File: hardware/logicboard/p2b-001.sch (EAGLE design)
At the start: 61 parts, among them IC1 74LS06N, IC2 4066N, J1 MKR, J2 GPIO, J3 Vcc, J4 RLY, J5 SPI, J6 LED, J7 DIN5, J8 DIN5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

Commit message: Signal name.
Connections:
- net N$4 renamed CAP1N
- net N$5 renamed CAP1P
- net N$7 renamed LCDVOUT
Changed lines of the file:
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@@
 </segment>
 </net>
-<net name="N$4" class="0">
+<net name="CAP1N" class="0">
 <segment>
 <pinref part="LCD1" gate="G$1" pin="3"/>
 <wire x1="332.74" y1="88.9" x2="358.14" y2="88.9" width="0.1524" layer="91"/>
 <pinref part="C12" gate="G$1" pin="2"/>
+<label x="345.44" y="88.9" size="1.778" layer="95"/>
 </segment>
 </net>
-<net name="N$5" class="0">
+<net name="CAP1P" class="0">
 <segment>
 <pinref part="LCD1" gate="G$1" pin="4"/>
@@
 <wire x1="322.58" y1="88.9" x2="325.12" y2="88.9" width="0.1524" layer="91"/>
 <pinref part="C12" gate="G$1" pin="1"/>
+<label x="345.44" y="86.36" size="1.778" layer="95"/>
 </segment>
 </net>
-<net name="N$7" class="0">
+<net name="LCDVOUT" class="0">
 <segment>
 <wire x1="332.74" y1="93.98" x2="335.28" y2="93.98" width="0.1524" layer="91"/>
@@
 <wire x1="335.28" y1="91.44" x2="358.14" y2="91.44" width="0.1524" layer="91"/>
 <pinref part="C13" gate="G$1" pin="2"/>
+<label x="345.44" y="91.44" size="1.778" layer="95"/>
 </segment>
 </net>

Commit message: Silk.
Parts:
- R101, R102: value (none) -> 10k
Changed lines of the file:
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@@
 <part name="JP7" library="pinhead" library_urn="urn:adsk.eagle:library:325" deviceset="PINHD-1X4" device="" package3d_urn="urn:adsk.eagle:package:22407/2" value="MNTR"/>
 <part name="LCD1" library="AQM0802A-RN-GBW" deviceset="AQM0802A-RN-GBW" device=""/>
-<part name="R101" library="rcl" library_urn="urn:adsk.eagle:library:334" deviceset="R-EU_" device="M2012" package3d_urn="urn:adsk.eagle:package:23561/2"/>
-<part name="R102" library="rcl" library_urn="urn:adsk.eagle:library:334" deviceset="R-EU_" device="M2012" package3d_urn="urn:adsk.eagle:package:23561/2"/>
+<part name="R101" library="rcl" library_urn="urn:adsk.eagle:library:334" deviceset="R-EU_" device="M2012" package3d_urn="urn:adsk.eagle:package:23561/2" value="10k"/>
+<part name="R102" library="rcl" library_urn="urn:adsk.eagle:library:334" deviceset="R-EU_" device="M2012" package3d_urn="urn:adsk.eagle:package:23561/2" value="10k"/>
 <part name="SUPPLY20" library="supply2" deviceset="GND" device=""/>
 <part name="C11" library="rcl" library_urn="urn:adsk.eagle:library:334" deviceset="C-EU" device="025-024X044" package3d_urn="urn:adsk.eagle:package:23630/1" value="100n"/>

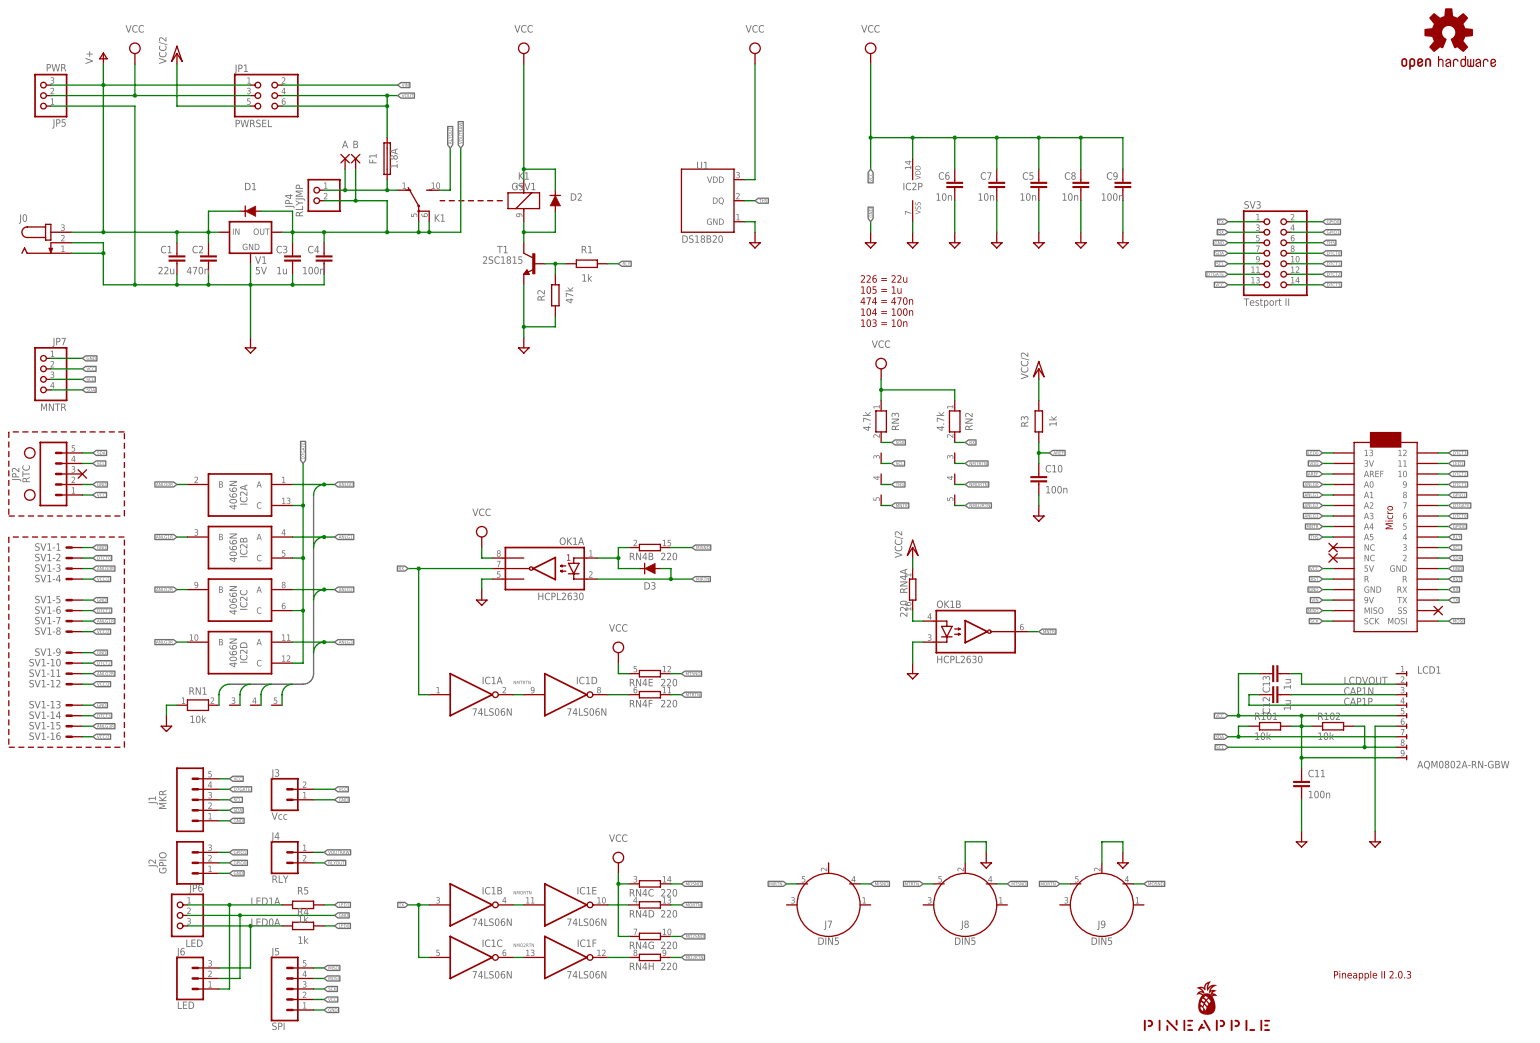
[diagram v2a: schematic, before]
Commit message: Now LCD runs on 5V or 3.3V.
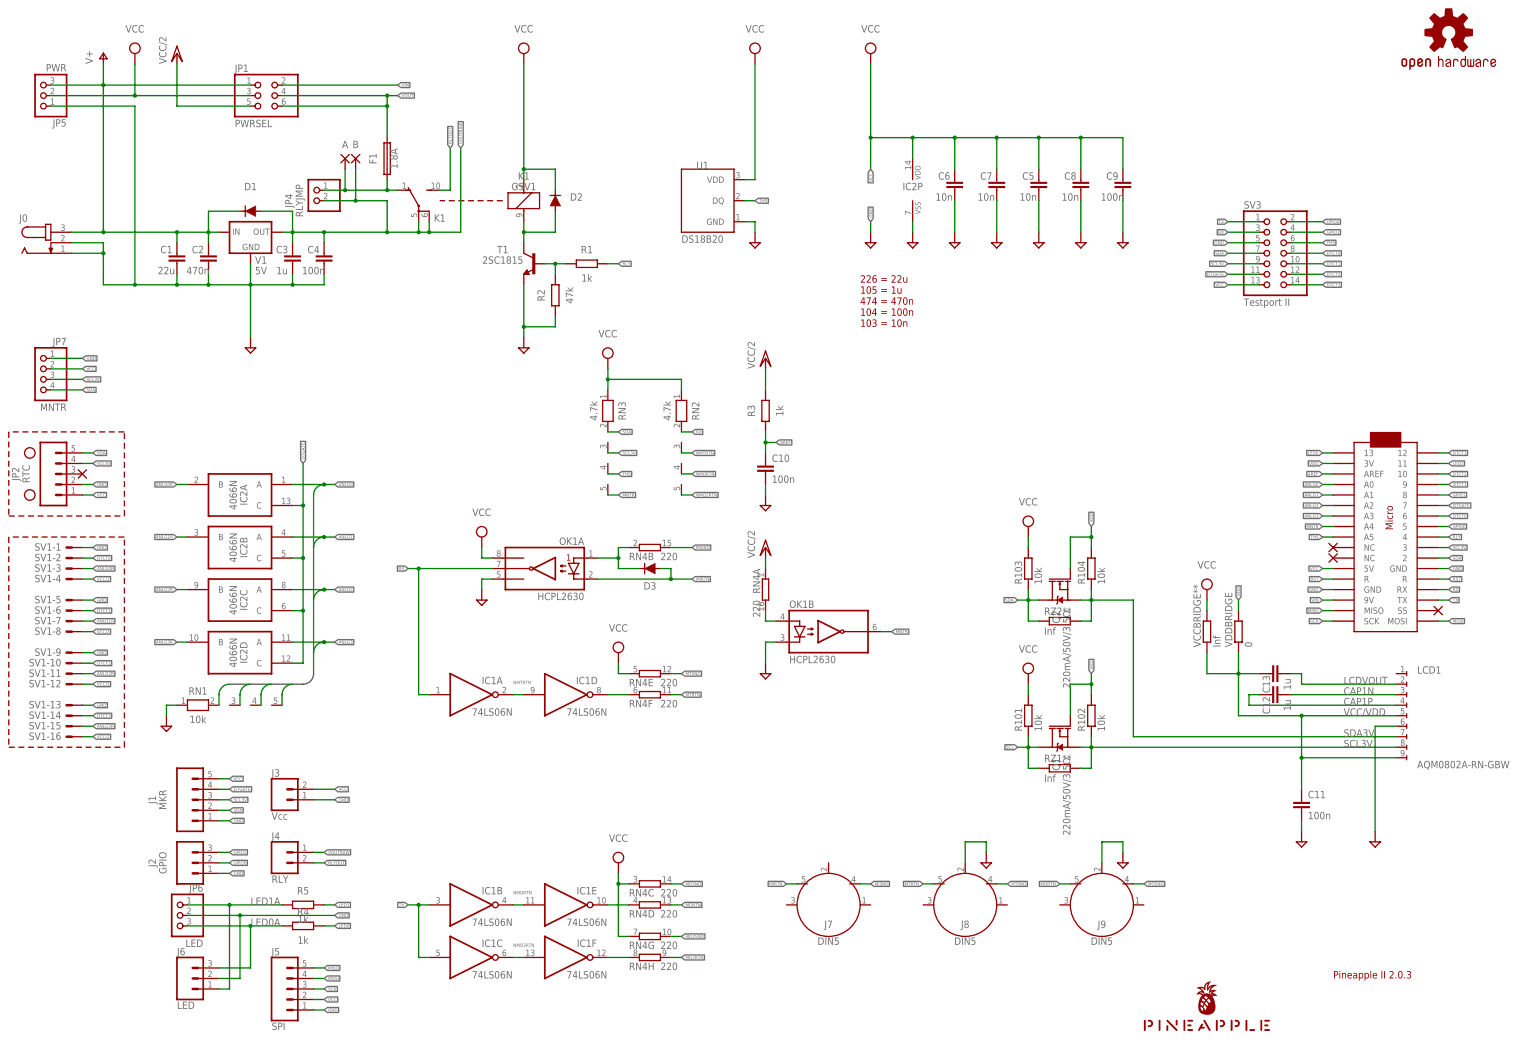
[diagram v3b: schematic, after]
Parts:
- added Q1, Q2: 220mA/50V/3.5Ω, SparkFun-DiscreteSemi:MOSFET-NCH-BSS138
- added R103, R104: 10k, rcl:R-EU_M2012
- added RZ1**, RZ2**, VCCBRIDGE**: Inf, rcl:R-EU_M2012
- added VDDBRIDGE: 0, rcl:R-EU_M2012
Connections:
- new net SCL3V: J1.3, JP2.4, JP7.3, LCD1.8, MC1.3, Q1.S, R102.1, RN3.3, RZ1**.2, SV3.9
- new net SDA3V: LCD1.7, Q2.S, R104.1, RZ2**.2
- new net VCC/VDD: C11.1, C13.1, LCD1.5, LCD1.9, VCCBRIDGE**.1, VDDBRIDGE.1
- net SCL: now also Q1.D, R101.1, RZ1**.1; no longer J1.3, JP2.4, JP7.3, LCD1.8, MC1.3, R102.2, RN3.3, SV3.9
- net SDA: now also Q2.D, R103.1, RZ2**.1; no longer LCD1.7, R101.1
- net VCC: now also R103.2, VCCBRIDGE**.2; no longer C11.1, C13.1, LCD1.5, LCD1.9, R102.1
- net VDD: now also Q1.G, Q2.G, R102.2, R104.2, VDDBRIDGE.2
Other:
- moved on the sheet: C10, C11, OK1B, R101, R102, R3, RN2, RN3, RN4A

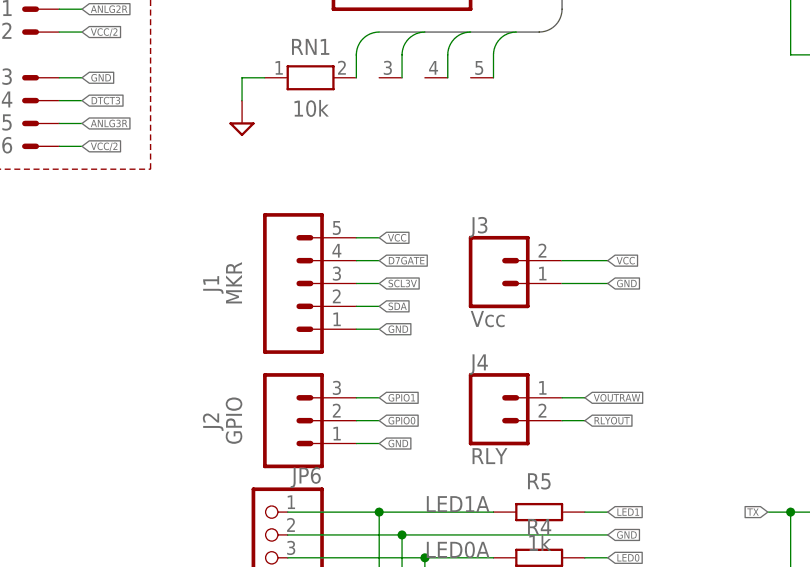
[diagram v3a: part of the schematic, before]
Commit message: Fixed silk and signal errors.
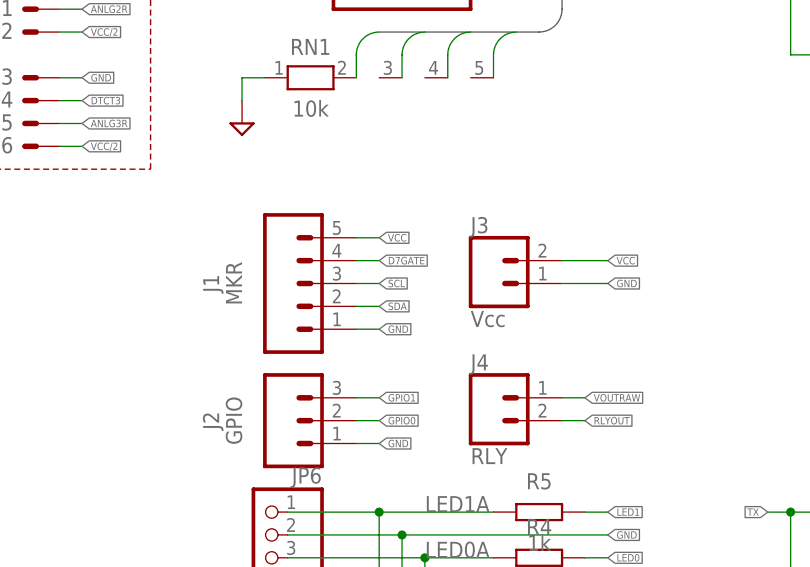
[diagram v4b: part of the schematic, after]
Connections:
- net SCL: now also J1.3
- net SCL3V: no longer J1.3
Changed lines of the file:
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@@
-</segment>
-<segment>
-<pinref part="J1" gate="G$1" pin="3"/>
-<wire x1="73.66" y1="63.5" x2="76.2" y2="63.5" width="0.1524" layer="91"/>
-<label x="76.2" y="63.5" size="0.8128" layer="95" xref="yes"/>
 </segment>
 <segment>
@@
 <wire x1="269.24" y1="71.12" x2="271.78" y2="71.12" width="0.1524" layer="91"/>
 </segment>
-</net>
+<segment>
+<pinref part="J1" gate="G$1" pin="3"/>
+<wire x1="73.66" y1="63.5" x2="76.2" y2="63.5" width="0.1524" layer="91"/>
+<label x="76.2" y="63.5" size="0.8128" layer="95" xref="yes"/>
+</segment>
+</net>

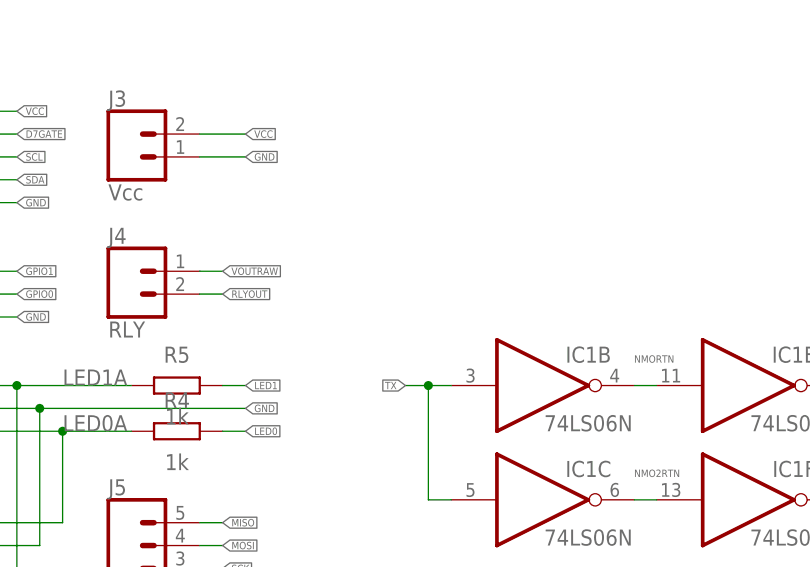
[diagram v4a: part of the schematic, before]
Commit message: Now has relay terminal as J42.
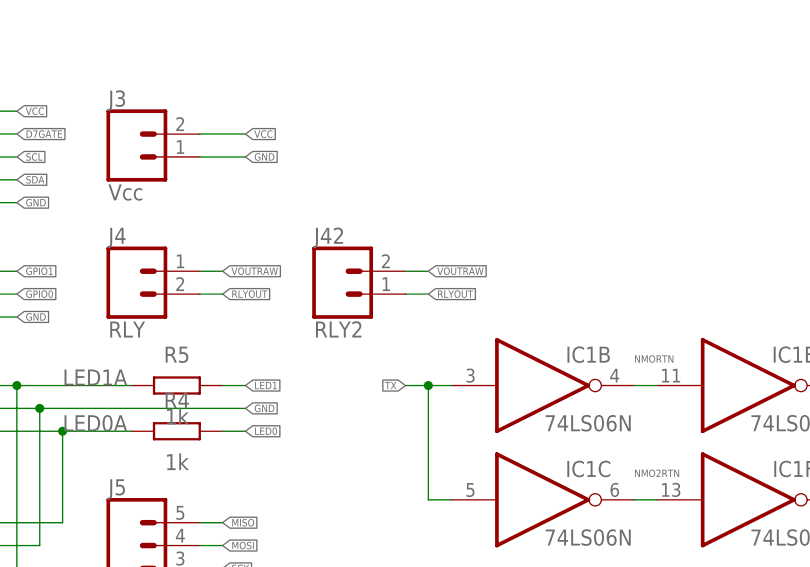
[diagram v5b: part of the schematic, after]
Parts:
- added J42: RLY2, SparkFun-Connectors:CONN_02JST-PTH-2
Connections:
- net RLYOUT: now also J42.1
- net VOUTRAW: now also J42.2
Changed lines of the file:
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@@
 <part name="VCCBRIDGE**" library="rcl" library_urn="urn:adsk.eagle:library:334" deviceset="R-EU_" device="M2012" package3d_urn="urn:adsk.eagle:package:23561/2" value="Inf"/>
 <part name="SUPPLY25" library="supply2" library_urn="urn:adsk.eagle:library:372" deviceset="VCC" device=""/>
+<part name="J42" library="SparkFun-Connectors" library_urn="urn:adsk.eagle:library:513" deviceset="CONN_02" device="JST-PTH-2" package3d_urn="urn:adsk.eagle:package:38053/1" value="RLY2"/>
 </parts>
 <sheets>
@@
 <instance part="SUPPLY25" gate="G$1" x="312.42" y="114.3" smashed="yes">
 <attribute name="VALUE" x="312.42" y="119.38" size="1.778" layer="96" align="bottom-center"/>
+</instance>
+<instance part="J42" gate="G$1" x="111.76" y="48.26" smashed="yes">
+<attribute name="VALUE" x="109.22" y="43.434" size="1.778" layer="96" font="vector"/>
+<attribute name="NAME" x="109.22" y="53.848" size="1.778" layer="95" font="vector"/>
 </instance>
 </instances>
@@
 <pinref part="J4" gate="G$1" pin="2"/>
 </segment>
+<segment>
+<wire x1="119.38" y1="50.8" x2="121.92" y2="50.8" width="0.1524" layer="91"/>
+<label x="121.92" y="50.8" size="0.8128" layer="95" xref="yes"/>
+<pinref part="J42" gate="G$1" pin="2"/>
+</segment>
 </net>
 <net name="RLYOUT" class="0">
@@
 <pinref part="J4" gate="G$1" pin="1"/>
 </segment>
-</net>
+<segment>
+<wire x1="119.38" y1="48.26" x2="121.92" y2="48.26" width="0.1524" layer="91"/>
+<label x="121.92" y="48.26" size="0.8128" layer="95" xref="yes"/>
+<pinref part="J42" gate="G$1" pin="1"/>
+</segment>
+</net>

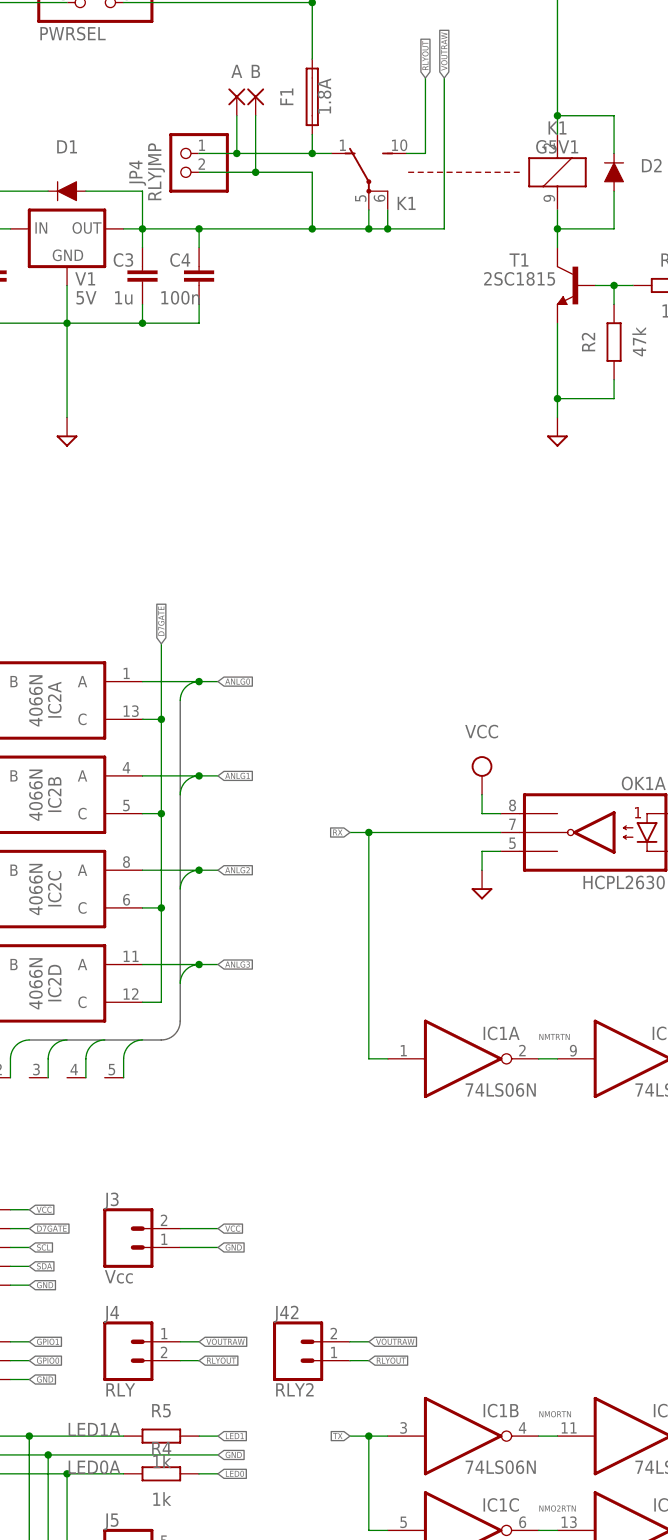
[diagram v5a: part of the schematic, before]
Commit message: 3-port relay terminal.
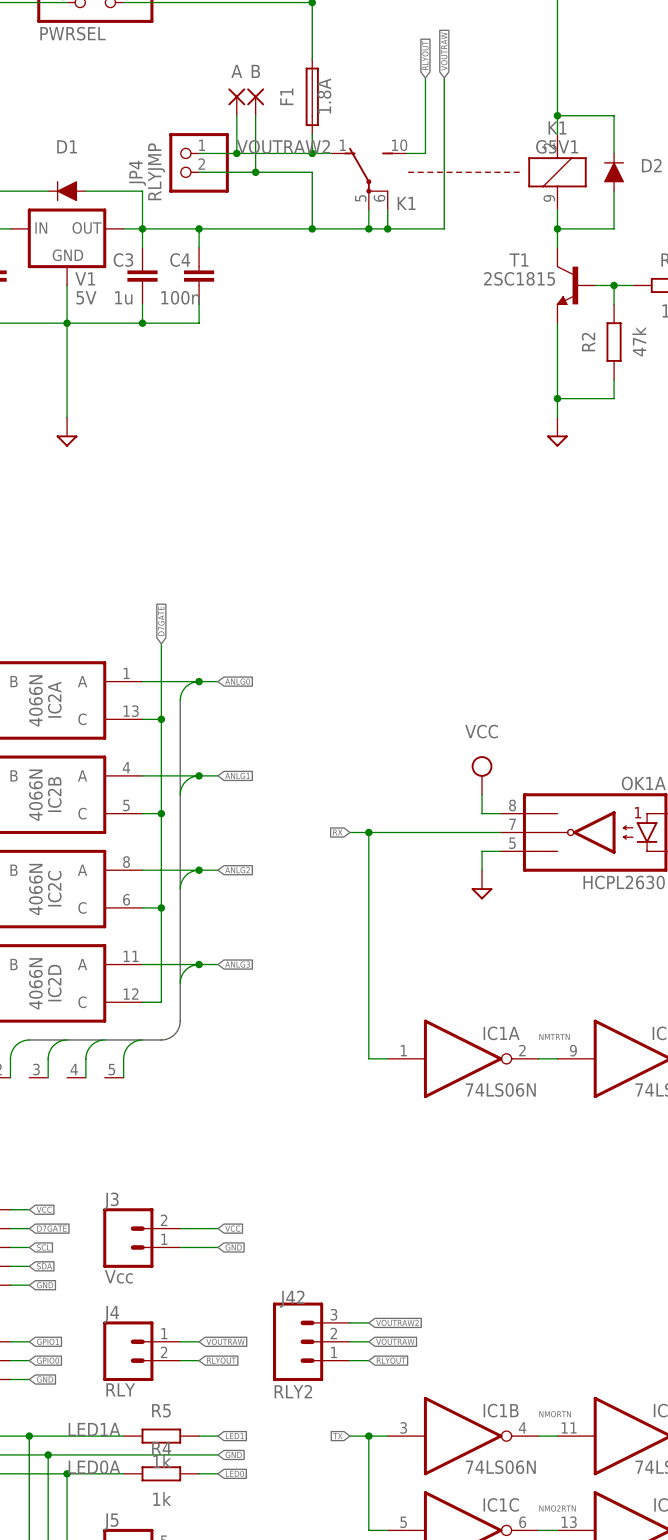
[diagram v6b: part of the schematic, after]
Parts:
- J42: device SparkFun-Connectors:CONN_02JST-PTH-2 -> SparkFun-Connectors:CONN_03JST-PTH
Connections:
- net VOUTRAW2: now also J42.3
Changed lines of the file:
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@@
 <part name="VCCBRIDGE**" library="rcl" library_urn="urn:adsk.eagle:library:334" deviceset="R-EU_" device="M2012" package3d_urn="urn:adsk.eagle:package:23561/2" value="Inf"/>
 <part name="SUPPLY25" library="supply2" library_urn="urn:adsk.eagle:library:372" deviceset="VCC" device=""/>
-<part name="J42" library="SparkFun-Connectors" library_urn="urn:adsk.eagle:library:513" deviceset="CONN_02" device="JST-PTH-2" package3d_urn="urn:adsk.eagle:package:38053/1" value="RLY2"/>
+<part name="J42" library="SparkFun-Connectors" library_urn="urn:adsk.eagle:library:513" deviceset="CONN_03" device="JST-PTH" package3d_urn="urn:adsk.eagle:package:38069/1" value="RLY2"/>
 </parts>
 <sheets>
@@
 <attribute name="VALUE" x="312.42" y="119.38" size="1.778" layer="96" align="bottom-center"/>
 </instance>
-<instance part="J42" gate="G$1" x="111.76" y="48.26" smashed="yes">
-<attribute name="VALUE" x="109.22" y="43.434" size="1.778" layer="96" font="vector"/>
-<attribute name="NAME" x="109.22" y="53.848" size="1.778" layer="95" font="vector"/>
+<instance part="J42" gate="J$1" x="111.76" y="50.8" smashed="yes">
+<attribute name="VALUE" x="111.76" y="43.18" size="1.778" layer="96" align="bottom-center"/>
+<attribute name="NAME" x="111.76" y="55.88" size="1.778" layer="95" align="bottom-center"/>
 </instance>
 </instances>
@@
 <wire x1="104.14" y1="215.9" x2="104.14" y2="210.82" width="0.1524" layer="91"/>
 <junction x="104.14" y="210.82"/>
+<label x="104.14" y="210.82" size="1.778" layer="95"/>
+</segment>
+<segment>
+<wire x1="121.92" y1="53.34" x2="119.38" y2="53.34" width="0.1524" layer="91"/>
+<label x="121.92" y="53.34" size="0.8128" layer="95" xref="yes"/>
+<pinref part="J42" gate="J$1" pin="3"/>
 </segment>
 </net>
@@
 <wire x1="119.38" y1="50.8" x2="121.92" y2="50.8" width="0.1524" layer="91"/>
 <label x="121.92" y="50.8" size="0.8128" layer="95" xref="yes"/>
-<pinref part="J42" gate="G$1" pin="2"/>
+<pinref part="J42" gate="J$1" pin="2"/>
 </segment>
 </net>
@@
 <wire x1="119.38" y1="48.26" x2="121.92" y2="48.26" width="0.1524" layer="91"/>
 <label x="121.92" y="48.26" size="0.8128" layer="95" xref="yes"/>
-<pinref part="J42" gate="G$1" pin="1"/>
-</segment>
-</net>
+<pinref part="J42" gate="J$1" pin="1"/>
+</segment>
+</net>
